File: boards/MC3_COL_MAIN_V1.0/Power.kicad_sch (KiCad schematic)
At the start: 12 parts, among them J1 SUPPLY_IN, Q1 AO4407C, U1 AMS1117-3.3

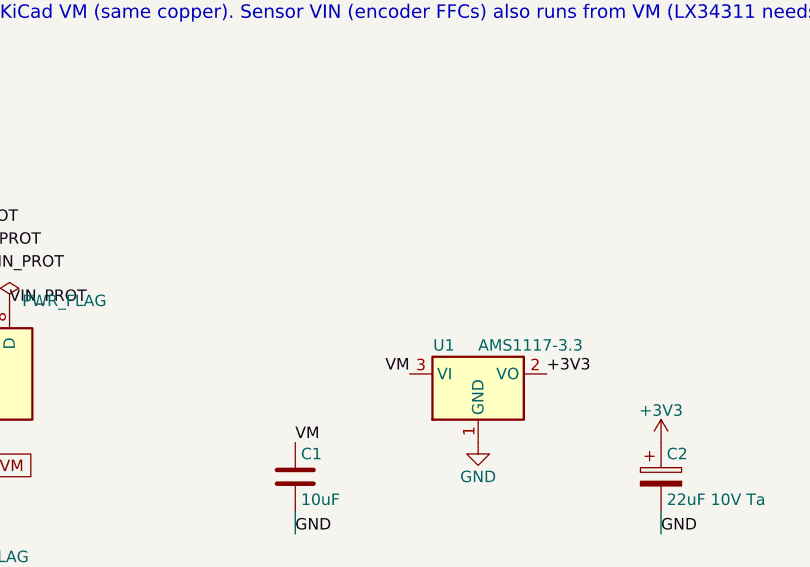
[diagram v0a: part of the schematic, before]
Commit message: Schematic: local VM bulk per channel + LDO input filter
Two changes to isolate motor switching noise from the +3V3 rail.

1. MotorChannel.kicad_sch gains a 10 uF 0805 (C15850) from VM to GND beside
   the existing 1 uF. One symbol in the shared sheet, so five caps on the
   board. TI asks for 0.1 uF plus bulk at VM and the board bulk was over in
   the power block, at the far end of the VM trunk.

2. Power.kicad_sch gains FB4 + C32 on a new VM_LDO net between VM and the
   AMS1117's VI pin, plus a PWR_FLAG the new net needs for ERC. The regulator
   was a direct path from the motor rail to +3V3 - its PSRR is down to about
   30 dB by 100 kHz, well inside the PWM band.

FB4 is C14709 (Murata BLM18PG121SN1D, 120R@100MHz, 2 A, 50 mohm), NOT the 600R
C1002 used on VDDA and VCAN5 - that part is 200 mA / 450 mohm and would have
been marginal on current and cost ~110 mV of the AMS1117's dropout headroom.

Flagged in MIGRATION: FB4 with C32 forms an LC at roughly 115 kHz with Q ~2.8,
which could amplify rather than attenuate if the motor PWM lands near it. Needs
the firmware's PWM frequency to close, and damping (tantalum or an R leg) if it
does - shrinking C32 would make it worse, not better.

ERC: 0 errors, the same 8 intentional same_local_global warnings as before.

Co-Authored-By: Claude Opus 5 (1M context) <noreply@anthropic.com>
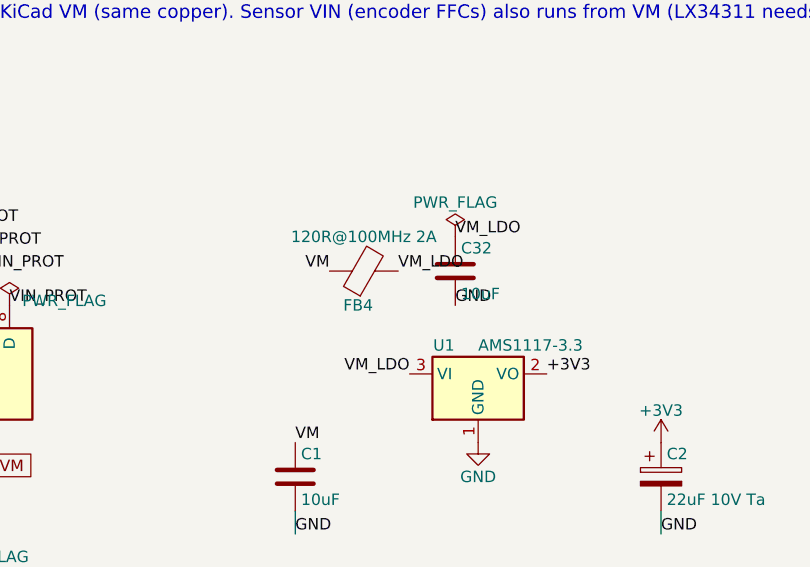
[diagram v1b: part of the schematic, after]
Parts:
- added C32: 10uF, MC3_COL_MAIN:C_0805_2012Metric, symbol Device:C
- added FB4: 120R@100MHz 2A, MC3_COL_MAIN:L_0603_1608Metric, symbol Device:FerriteBead
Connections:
- net GND: now also C32.2
- net VM: now also FB4.1; no longer U1.3 (VI)
- new net VM_LDO: C32.1, FB4.2, U1.3 (VI)
